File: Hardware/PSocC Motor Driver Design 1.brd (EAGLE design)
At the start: 25.4 x 25.4 mm, 41 parts

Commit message: Sending it home
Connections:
- new net P2.3: U$1.4, U$2.11
- net P2.0: no longer U$2.11
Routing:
- net VCC: track 56.9 -> 59.2 mm
- net P2.3: track 0.00 -> 2.30 mm
- net P2.0: track 3.36 -> 3.64 mm, vias 0 -> 1
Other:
- board text added: "TODO: Fix PSoC aperatures"
- board text added: "v11"
- board text removed: "TODO: Fix DRV cream layer"
- board text removed: "v20"
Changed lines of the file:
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@@
 <layer number="29" name="tStop" color="7" fill="3" visible="no" active="yes"/>
 <layer number="30" name="bStop" color="7" fill="6" visible="no" active="yes"/>
-<layer number="31" name="tCream" color="7" fill="4" visible="no" active="yes"/>
+<layer number="31" name="tCream" color="7" fill="4" visible="yes" active="yes"/>
 <layer number="32" name="bCream" color="7" fill="5" visible="no" active="yes"/>
 <layer number="33" name="tFinish" color="6" fill="3" visible="no" active="yes"/>
@@
 <layer number="45" name="Holes" color="7" fill="1" visible="yes" active="yes"/>
 <layer number="46" name="Milling" color="3" fill="1" visible="no" active="yes"/>
-<layer number="47" name="Measures" color="7" fill="1" visible="yes" active="yes"/>
+<layer number="47" name="Measures" color="7" fill="1" visible="no" active="yes"/>
 <layer number="48" name="Document" color="7" fill="1" visible="no" active="yes"/>
 <layer number="49" name="Reference" color="7" fill="1" visible="no" active="yes"/>
@@
 <text x="7.9771875" y="18.2165625" size="0.8128" layer="22" font="vector" ratio="15" rot="MR0" align="center">Pull Enb</text>
 <text x="27.94" y="22.86" size="0.8128" layer="21" align="center-left">TODO:
-Fix DRV cream layer
+Fix PSoC aperatures
 </text>
 <text x="13.096875" y="-18.1371875" size="1.778" layer="51" font="vector" align="center-left">Marshall Taylor</text>
@@
 <text x="3.6115625" y="0.79375" size="0.8128" layer="22" font="vector" ratio="15" rot="MR0" align="center-left">GND</text>
 <text x="17.859375" y="5.476875" size="0.8128" layer="22" font="vector" ratio="15" rot="MR0" align="center-left">VREG</text>
-<text x="7.8978125" y="0.2778125" size="1.016" layer="16" font="vector" ratio="15" rot="MR0">v20</text>
+<text x="7.8978125" y="0.2778125" size="1.016" layer="16" font="vector" ratio="15" rot="MR0">v11</text>
 <text x="9.04875" y="8.969375" size="0.8128" layer="21" font="vector" ratio="15" align="center-left">PROG</text>
 <dimension x1="-1.27" y1="22.86" x2="-1.27" y2="0" x3="-3.81" y3="11.43" textsize="1.778" textratio="15" layer="47" dtype="vertical" unit="inch"/>
@@
 <wire x1="6.5484375" y1="11.0728125" x2="6.1515625" y2="11.4696875" width="0.4064" layer="1"/>
 <contactref element="C12" pad="-"/>
-<via x="16.5496875" y="8.0565625" extent="1-16" drill="0.381"/>
+<via x="15.8353125" y="7.381875" extent="1-16" drill="0.381"/>
 <via x="21.59" y="6.35" extent="1-16" drill="0.381"/>
 <via x="11.43" y="1.27" extent="1-16" drill="0.381"/>
 <via x="24.13" y="20.32" extent="1-16" drill="0.381"/>
 <via x="2.54" y="6.35" extent="1-16" drill="0.381"/>
-<via x="16.51" y="11.43" extent="1-16" drill="0.381"/>
+<via x="15.24" y="10.9140625" extent="1-16" drill="0.381"/>
 <via x="19.05" y="18.6928125" extent="1-16" drill="0.381"/>
 <via x="19.84375" y="10.1203125" extent="1-16" drill="0.381"/>
@@
 <wire x1="5.55625" y1="6.0721875" x2="6.8659375" y2="4.7625" width="0.4064" layer="16"/>
 <wire x1="6.8659375" y1="4.7625" x2="12.303125" y2="4.7625" width="0.4064" layer="16"/>
-<via x="17.541875" y="10.1203125" extent="1-16" drill="0.381"/>
+<via x="15.954375" y="8.493125" extent="1-16" drill="0.381"/>
 <wire x1="12.303125" y1="4.7625" x2="14.049375" y2="4.7625" width="0.4064" layer="16"/>
-<wire x1="17.541875" y1="10.1203125" x2="17.224375" y2="9.8028125" width="0.4064" layer="1"/>
-<wire x1="17.224375" y1="9.8028125" x2="16.09" y2="9.8028125" width="0.4064" layer="1"/>
+<wire x1="16.8275" y1="9.8028125" x2="16.09" y2="9.8028125" width="0.4064" layer="1"/>
 <contactref element="J3" pad="1"/>
 <via x="12.303125" y="4.7625" extent="1-16" drill="0.381"/>
 <wire x1="18" y1="15.26" x2="17.4825" y2="15.26" width="0.254" layer="1"/>
 <wire x1="17.4825" y1="15.26" x2="17.30375" y2="15.08125" width="0.254" layer="1"/>
-<wire x1="17.30375" y1="15.08125" x2="17.30375" y2="14.049375" width="0.254" layer="1"/>
-<wire x1="17.30375" y1="14.049375" x2="16.8671875" y2="13.6128125" width="0.254" layer="1"/>
-<wire x1="16.8671875" y1="13.6128125" x2="16.8671875" y2="12.7396875" width="0.254" layer="1"/>
-<via x="16.8671875" y="12.7396875" extent="1-16" drill="0.381"/>
-<wire x1="16.8671875" y1="12.7396875" x2="17.541875" y2="12.065" width="0.254" layer="16"/>
-<wire x1="17.541875" y1="12.065" x2="17.541875" y2="10.1203125" width="0.254" layer="16"/>
+<via x="17.8831875" y="13.7556875" extent="1-16" drill="0.381"/>
 <wire x1="5.55625" y1="7.4215625" x2="5.55625" y2="8.6353125" width="0.4064" layer="1"/>
 <wire x1="5.55625" y1="8.6353125" x2="5.5959375" y2="8.6353125" width="0.4064" layer="1"/>
@@
 <wire x1="14.049375" y1="4.7625" x2="18.7325" y2="4.7625" width="0.4064" layer="16"/>
 <wire x1="18.7325" y1="4.7625" x2="19.05" y2="5.08" width="0.4064" layer="16"/>
-<wire x1="14.049375" y1="5.318125" x2="14.843125" y2="6.111875" width="0.254" layer="16"/>
-<wire x1="14.843125" y1="6.111875" x2="14.843125" y2="8.493125" width="0.254" layer="16"/>
-<wire x1="14.843125" y1="8.493125" x2="16.4703125" y2="10.1203125" width="0.254" layer="16"/>
-<wire x1="16.4703125" y1="10.1203125" x2="17.541875" y2="10.1203125" width="0.254" layer="16"/>
+<wire x1="14.049375" y1="5.318125" x2="14.9304375" y2="6.1991875" width="0.4064" layer="16"/>
 <wire x1="12.303125" y1="4.7625" x2="12.303125" y2="5.3975" width="0.254" layer="1"/>
 <wire x1="12.303125" y1="5.3975" x2="12.461875" y2="5.55625" width="0.254" layer="1"/>
@@
 <wire x1="13.49375" y1="5.9928125" x2="13.49375" y2="6.82625" width="0.254" layer="1"/>
 <wire x1="13.49375" y1="6.82625" x2="12.7" y2="7.62" width="0.254" layer="1"/>
-<wire x1="14.049375" y1="5.318125" x2="14.049375" y2="4.7625" width="0.254" layer="16"/>
+<wire x1="14.049375" y1="5.318125" x2="14.049375" y2="4.7625" width="0.4064" layer="16"/>
 <contactref element="JP5" pad="2"/>
 <wire x1="5.5959375" y1="8.6353125" x2="6.4921875" y2="8.6353125" width="0.254" layer="1"/>
@@
 <wire x1="8.255" y1="15.2796875" x2="8.255" y2="16.51" width="0.254" layer="16"/>
 <wire x1="9.0884375" y1="9.2471875" x2="9.3265625" y2="9.0090625" width="0.254" layer="16"/>
+<wire x1="17.30375" y1="15.08125" x2="17.30375" y2="13.93825" width="0.254" layer="1"/>
+<wire x1="17.30375" y1="13.93825" x2="17.4863125" y2="13.7556875" width="0.254" layer="1"/>
+<wire x1="17.8831875" y1="13.7556875" x2="17.4863125" y2="13.7556875" width="0.254" layer="1"/>
+<wire x1="17.541875" y1="13.414375" x2="17.8831875" y2="13.7556875" width="0.254" layer="16"/>
+<wire x1="14.9304375" y1="6.1991875" x2="14.9304375" y2="8.22325" width="0.4064" layer="16"/>
+<wire x1="14.9304375" y1="8.22325" x2="15.2003125" y2="8.493125" width="0.4064" layer="16"/>
+<wire x1="15.2003125" y1="8.493125" x2="15.954375" y2="8.493125" width="0.4064" layer="16"/>
+<wire x1="15.954375" y1="8.493125" x2="16.8275" y2="8.493125" width="0.4064" layer="1"/>
+<wire x1="16.8275" y1="8.493125" x2="17.0259375" y2="8.6915625" width="0.4064" layer="1"/>
+<wire x1="17.0259375" y1="8.6915625" x2="17.0259375" y2="9.604375" width="0.4064" layer="1"/>
+<wire x1="17.0259375" y1="9.604375" x2="16.8275" y2="9.8028125" width="0.4064" layer="1"/>
+<wire x1="17.541875" y1="13.414375" x2="17.224375" y2="13.414375" width="0.254" layer="16"/>
+<wire x1="17.224375" y1="13.414375" x2="15.9940625" y2="12.1840625" width="0.254" layer="16"/>
+<wire x1="15.9940625" y1="12.1840625" x2="15.9940625" y2="11.3109375" width="0.254" layer="16"/>
+<wire x1="15.9940625" y1="11.3109375" x2="16.7878125" y2="10.5171875" width="0.254" layer="16"/>
+<wire x1="16.7878125" y1="10.5171875" x2="16.7878125" y2="9.3265625" width="0.254" layer="16"/>
+<wire x1="16.7878125" y1="9.3265625" x2="15.954375" y2="8.493125" width="0.254" layer="16"/>
 </signal>
 <signal name="!RESET">
@@
 <wire x1="13.5334375" y1="21.9075" x2="13.5334375" y2="20.9153125" width="0.254" layer="16"/>
 <wire x1="13.5334375" y1="20.9153125" x2="14.366875" y2="20.081875" width="0.254" layer="16"/>
-</signal>
-<signal name="P2.0">
-<contactref element="U$1" pad="1"/>
-<contactref element="U$2" pad="11"/>
-<wire x1="15.7" y1="14.26" x2="16.403125" y2="14.26" width="0.254" layer="1"/>
-<wire x1="16.403125" y1="14.26" x2="16.748125" y2="14.605" width="0.254" layer="1"/>
-<wire x1="16.748125" y1="14.605" x2="16.748125" y2="15.3590625" width="0.254" layer="1"/>
-<wire x1="16.748125" y1="15.3590625" x2="17.145" y2="15.7559375" width="0.254" layer="1"/>
-<wire x1="17.145" y1="15.7559375" x2="17.9959375" y2="15.7559375" width="0.254" layer="1"/>
-<wire x1="17.9959375" y1="15.7559375" x2="18" y2="15.76" width="0.254" layer="1"/>
 </signal>
 <signal name="VIN">
@@
 <wire x1="13.95" y1="20.935" x2="14.366875" y2="21.351875" width="0.254" layer="1"/>
 </signal>
+<signal name="P2.3">
+<contactref element="U$1" pad="4"/>
+<contactref element="U$2" pad="11"/>
+<wire x1="17.9959375" y1="15.7559375" x2="18" y2="15.76" width="0.254" layer="1"/>
+<wire x1="17.9959375" y1="15.7559375" x2="15.7040625" y2="15.7559375" width="0.254" layer="1"/>
+<wire x1="15.7040625" y1="15.7559375" x2="15.7" y2="15.76" width="0.254" layer="1"/>
+</signal>
+<signal name="P2.0">
+<contactref element="U$1" pad="1"/>
+<via x="16.748125" y="11.7475" extent="1-16" drill="0.381"/>
+<wire x1="16.748125" y1="11.7475" x2="16.1925" y2="12.303125" width="0.254" layer="1"/>
+<wire x1="16.1925" y1="12.303125" x2="16.1925" y2="13.0571875" width="0.254" layer="1"/>
+<wire x1="16.1925" y1="13.0571875" x2="16.5496875" y2="13.414375" width="0.254" layer="1"/>
+<wire x1="16.5496875" y1="13.414375" x2="16.5496875" y2="14.0890625" width="0.254" layer="1"/>
+<wire x1="16.5496875" y1="14.0890625" x2="16.37875" y2="14.26" width="0.254" layer="1"/>
+<wire x1="16.37875" y1="14.26" x2="15.7" y2="14.26" width="0.254" layer="1"/>
+</signal>
 </signals>

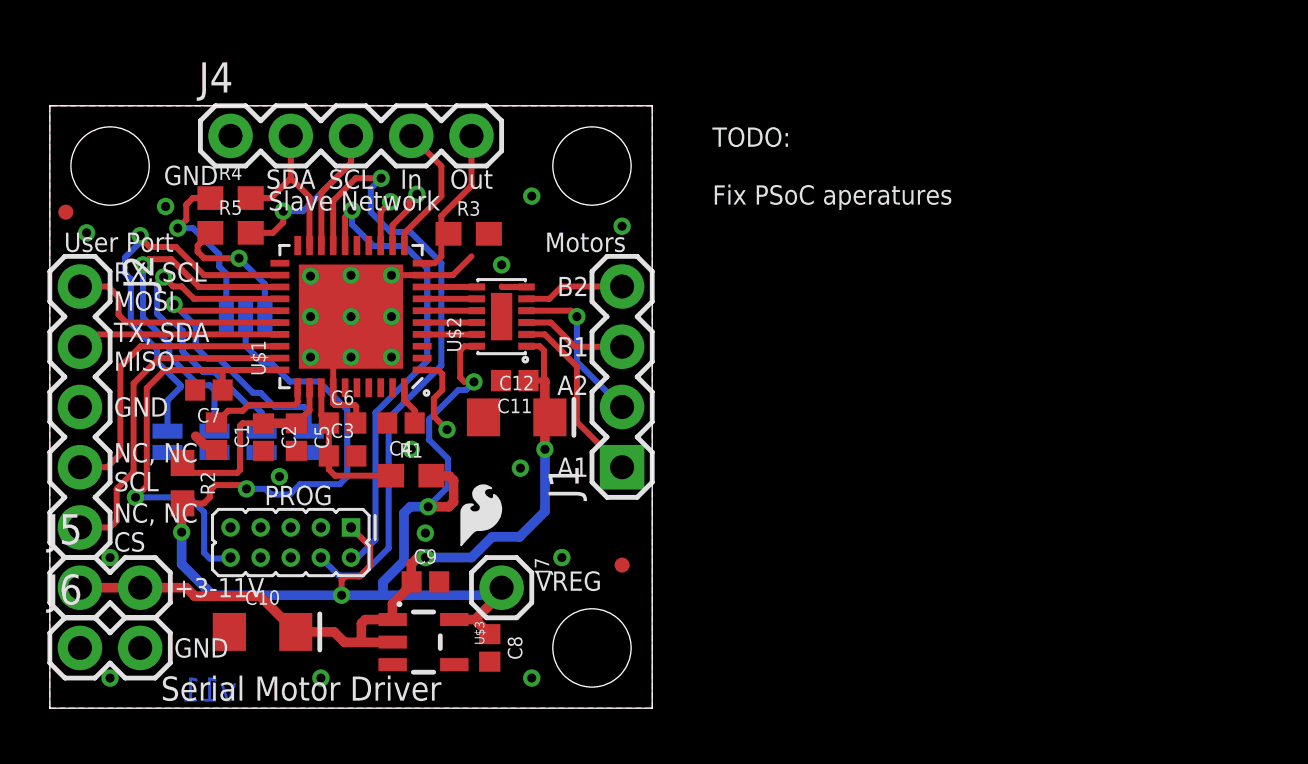
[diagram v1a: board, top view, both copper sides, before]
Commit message: Working on checklist
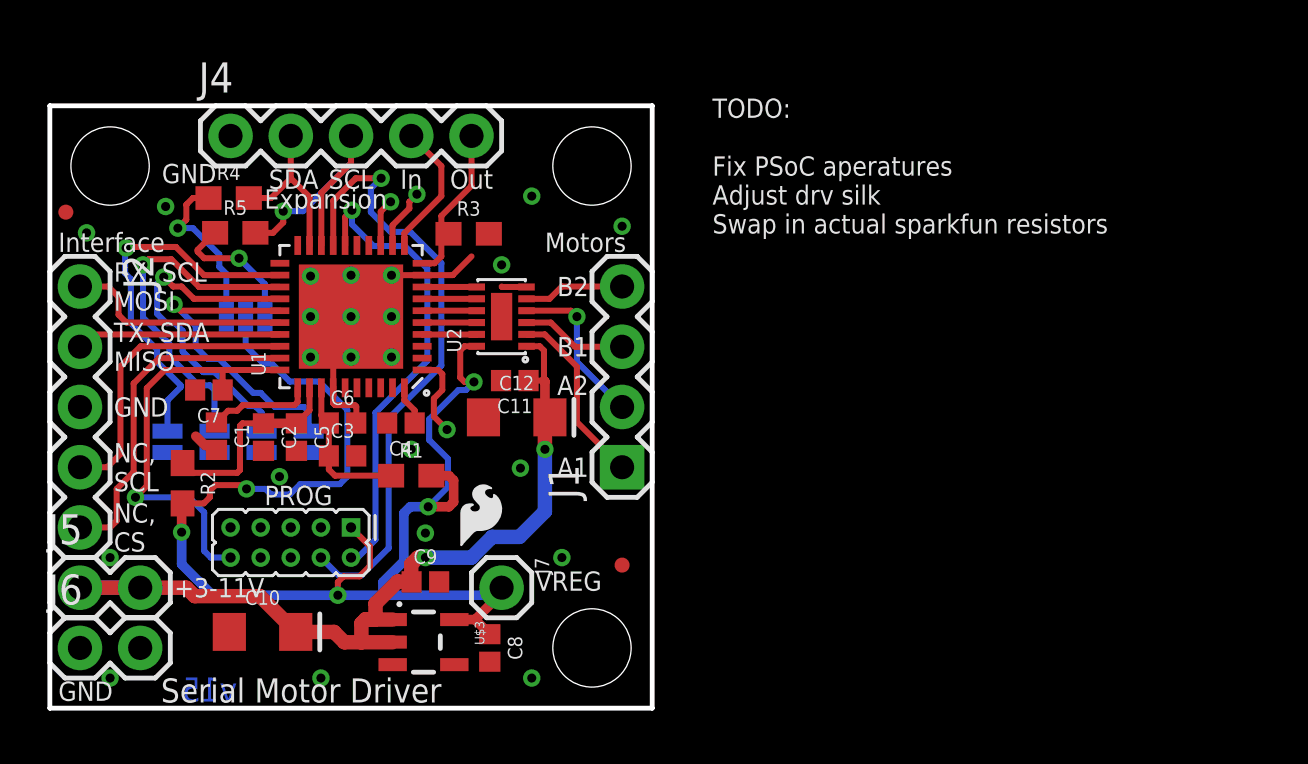
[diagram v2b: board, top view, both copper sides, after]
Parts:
- JP1, JP2, JP3, JP4: value JUMPER-PAD-2-NOYES_SILK -> JUMPER-PAD-2
- moved R5 0.20 mm to (7.82, 20.0)
- moved R4 0.08 mm to (7.54, 21.5)
- renumbered U$1 to U1, U$2 to U2
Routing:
- net VIN: track 34.1 -> 37.9 mm
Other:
- board text added: "(bridge='1')"
- board text added: "Expansion"
- board text added: "Interface"
- board text added: "Measurements in inches."
- board text added: "NC, CS"
- board text added: "NC, SCL"
- board text added: "TODO: Fix PSoC aperatures Adjust drv silk Swap in actual sparkfun resistors"
- board text added: "v15"
- board text removed: "All measurements in inches."
- board text removed: "NC, NC CS"
- board text removed: "NC, NC SCL"
- board text removed: "Slave Network"
- board text removed: "TODO: Fix PSoC aperatures"
- board text removed: "User Port"
- board text removed: "v11"

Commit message: Finished checklist
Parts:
- added D1: RED, SparkFun-LED:LED-0603
- added R6: 470, SparkFun-Resistors:0603
- J1, J2, J3, J4, J5, J6, J7: value (none) -> DNP
- R3, R4, R5: value 1 -> 4.7k
- U1: device SparkFun-DigitalIC:QFN-40 -> PSOC4TempLib:QFN-40
- moved LOGO1 5.64 mm to (22.6, 5.75)
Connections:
- new net N$10: D1.A, R6.2
- net GND: now also D1.C
- net P2.0: now also R6.1
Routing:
- net P2.0: track 3.64 -> 8.77 mm, vias 1 -> 2
- net N$10: track 0.00 -> 2.89 mm
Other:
- board text added: "STAT"
- board text removed: "TODO: Fix PSoC aperatures Adjust drv silk Swap in actual sparkfun resistors"
